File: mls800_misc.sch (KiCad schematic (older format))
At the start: 18 parts, among them SW10 SW_TACT_LED_2, SW11 SW_TACT_LED_2, SW4 SW_TACT_LED_2, SW5 SW_TACT_LED_2, SW6 SW_TACT_LED_2, SW7 SW_TACT_LED_2, SW8 SW_TACT_LED_2, SW9 SW_TACT_LED_2, U4 MCP23017

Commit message: MLS800 : fixed missing components
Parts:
- SW10, SW11, SW4, SW5, SW6, SW7, SW8, SW9: value SW_TACT_LED_2 -> SW_TACT_LED; symbol SW_TACT_LED_2 -> SW_TACT_LED
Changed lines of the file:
@@
 LIBS:custom-device
 LIBS:custom-display
+LIBS:custom-micro
 LIBS:mls800-cache
 EELAYER 24 0
@@
 	3600 4850 3700 4950
 $Comp
-L SW_TACT_LED_2 SW4
+L SW_TACT_LED SW4
 U 2 1 53B9BB32
 P 4900 1300
 F 0 "SW4" H 4700 1200 60  0000 C CNN
-F 1 "SW_TACT_LED_2" H 4950 1200 60  0001 C CNN
+F 1 "SW_TACT_LED" H 4950 1200 60  0001 C CNN
 F 2 "" H 4900 1300 60  0000 C CNN
 F 3 "" H 4900 1300 60  0000 C CNN
@@
 $EndComp
 $Comp
-L SW_TACT_LED_2 SW4
+L SW_TACT_LED SW4
 U 1 1 53B9BB41
 P 4900 1100
 F 0 "SW4" H 4700 1250 60  0000 C CNN
-F 1 "SW_TACT_LED_2" H 4950 1000 60  0001 C CNN
+F 1 "SW_TACT_LED" H 4950 1000 60  0001 C CNN
 F 2 "" H 4900 1100 60  0000 C CNN
 F 3 "" H 4900 1100 60  0000 C CNN
@@
 $EndComp
 $Comp
-L SW_TACT_LED_2 SW5
+L SW_TACT_LED SW5
 U 2 1 53B9BB96
 P 4900 1850
 F 0 "SW5" H 4700 1750 60  0000 C CNN
-F 1 "SW_TACT_LED_2" H 4950 1750 60  0001 C CNN
+F 1 "SW_TACT_LED" H 4950 1750 60  0001 C CNN
 F 2 "" H 4900 1850 60  0000 C CNN
 F 3 "" H 4900 1850 60  0000 C CNN
@@
 $EndComp
 $Comp
-L SW_TACT_LED_2 SW5
+L SW_TACT_LED SW5
 U 1 1 53B9BB9C
 P 4900 1650
 F 0 "SW5" H 4700 1800 60  0000 C CNN
-F 1 "SW_TACT_LED_2" H 4950 1550 60  0001 C CNN
+F 1 "SW_TACT_LED" H 4950 1550 60  0001 C CNN
 F 2 "" H 4900 1650 60  0000 C CNN
 F 3 "" H 4900 1650 60  0000 C CNN
@@
 $EndComp
 $Comp
-L SW_TACT_LED_2 SW6
+L SW_TACT_LED SW6
 U 2 1 53B9BBAC
 P 4900 2400
 F 0 "SW6" H 4700 2300 60  0000 C CNN
-F 1 "SW_TACT_LED_2" H 4950 2300 60  0001 C CNN
+F 1 "SW_TACT_LED" H 4950 2300 60  0001 C CNN
 F 2 "" H 4900 2400 60  0000 C CNN
 F 3 "" H 4900 2400 60  0000 C CNN
@@
 $EndComp
 $Comp
-L SW_TACT_LED_2 SW6
+L SW_TACT_LED SW6
 U 1 1 53B9BBB2
 P 4900 2200
 F 0 "SW6" H 4700 2350 60  0000 C CNN
-F 1 "SW_TACT_LED_2" H 4950 2100 60  0001 C CNN
+F 1 "SW_TACT_LED" H 4950 2100 60  0001 C CNN
 F 2 "" H 4900 2200 60  0000 C CNN
 F 3 "" H 4900 2200 60  0000 C CNN
@@
 $EndComp
 $Comp
-L SW_TACT_LED_2 SW7
+L SW_TACT_LED SW7
 U 2 1 53B9BBB8
 P 4900 2950
 F 0 "SW7" H 4700 2850 60  0000 C CNN
-F 1 "SW_TACT_LED_2" H 4950 2850 60  0001 C CNN
+F 1 "SW_TACT_LED" H 4950 2850 60  0001 C CNN
 F 2 "" H 4900 2950 60  0000 C CNN
 F 3 "" H 4900 2950 60  0000 C CNN
@@
 $EndComp
 $Comp
-L SW_TACT_LED_2 SW7
+L SW_TACT_LED SW7
 U 1 1 53B9BBBE
 P 4900 2750
 F 0 "SW7" H 4700 2900 60  0000 C CNN
-F 1 "SW_TACT_LED_2" H 4950 2650 60  0001 C CNN
+F 1 "SW_TACT_LED" H 4950 2650 60  0001 C CNN
 F 2 "" H 4900 2750 60  0000 C CNN
 F 3 "" H 4900 2750 60  0000 C CNN
@@
 $EndComp
 $Comp
-L SW_TACT_LED_2 SW8
+L SW_TACT_LED SW8
 U 2 1 53B9BBC4
 P 4900 3500
 F 0 "SW8" H 4700 3400 60  0000 C CNN
-F 1 "SW_TACT_LED_2" H 4950 3400 60  0001 C CNN
+F 1 "SW_TACT_LED" H 4950 3400 60  0001 C CNN
 F 2 "" H 4900 3500 60  0000 C CNN
 F 3 "" H 4900 3500 60  0000 C CNN
@@
 $EndComp
 $Comp
-L SW_TACT_LED_2 SW8
+L SW_TACT_LED SW8
 U 1 1 53B9BBCA
 P 4900 3300
 F 0 "SW8" H 4700 3450 60  0000 C CNN
-F 1 "SW_TACT_LED_2" H 4950 3200 60  0001 C CNN
+F 1 "SW_TACT_LED" H 4950 3200 60  0001 C CNN
 F 2 "" H 4900 3300 60  0000 C CNN
 F 3 "" H 4900 3300 60  0000 C CNN
@@
 $EndComp
 $Comp
-L SW_TACT_LED_2 SW9
+L SW_TACT_LED SW9
 U 2 1 53B9BBD0
 P 4900 4050
 F 0 "SW9" H 4700 3950 60  0000 C CNN
-F 1 "SW_TACT_LED_2" H 4950 3950 60  0001 C CNN
+F 1 "SW_TACT_LED" H 4950 3950 60  0001 C CNN
 F 2 "" H 4900 4050 60  0000 C CNN
 F 3 "" H 4900 4050 60  0000 C CNN
@@
 $EndComp
 $Comp
-L SW_TACT_LED_2 SW9
+L SW_TACT_LED SW9
 U 1 1 53B9BBD6
 P 4900 3850
 F 0 "SW9" H 4700 4000 60  0000 C CNN
-F 1 "SW_TACT_LED_2" H 4950 3750 60  0001 C CNN
+F 1 "SW_TACT_LED" H 4950 3750 60  0001 C CNN
 F 2 "" H 4900 3850 60  0000 C CNN
 F 3 "" H 4900 3850 60  0000 C CNN
@@
 $EndComp
 $Comp
-L SW_TACT_LED_2 SW10
+L SW_TACT_LED SW10
 U 2 1 53B9BBDC
 P 4900 4600
 F 0 "SW10" H 4700 4500 60  0000 C CNN
-F 1 "SW_TACT_LED_2" H 4950 4500 60  0001 C CNN
+F 1 "SW_TACT_LED" H 4950 4500 60  0001 C CNN
 F 2 "" H 4900 4600 60  0000 C CNN
 F 3 "" H 4900 4600 60  0000 C CNN
@@
 $EndComp
 $Comp
-L SW_TACT_LED_2 SW10
+L SW_TACT_LED SW10
 U 1 1 53B9BBE2
 P 4900 4400
 F 0 "SW10" H 4700 4550 60  0000 C CNN
-F 1 "SW_TACT_LED_2" H 4950 4300 60  0001 C CNN
+F 1 "SW_TACT_LED" H 4950 4300 60  0001 C CNN
 F 2 "" H 4900 4400 60  0000 C CNN
 F 3 "" H 4900 4400 60  0000 C CNN
@@
 $EndComp
 $Comp
-L SW_TACT_LED_2 SW11
+L SW_TACT_LED SW11
 U 2 1 53B9BBE8
 P 4900 5150
 F 0 "SW11" H 4700 5050 60  0000 C CNN
-F 1 "SW_TACT_LED_2" H 4950 5050 60  0001 C CNN
+F 1 "SW_TACT_LED" H 4950 5050 60  0001 C CNN
 F 2 "" H 4900 5150 60  0000 C CNN
 F 3 "" H 4900 5150 60  0000 C CNN
@@
 $EndComp
 $Comp
-L SW_TACT_LED_2 SW11
+L SW_TACT_LED SW11
 U 1 1 53B9BBEE
 P 4900 4950
 F 0 "SW11" H 4700 5100 60  0000 C CNN
-F 1 "SW_TACT_LED_2" H 4950 4850 60  0001 C CNN
+F 1 "SW_TACT_LED" H 4950 4850 60  0001 C CNN
 F 2 "" H 4900 4950 60  0000 C CNN
 F 3 "" H 4900 4950 60  0000 C CNN

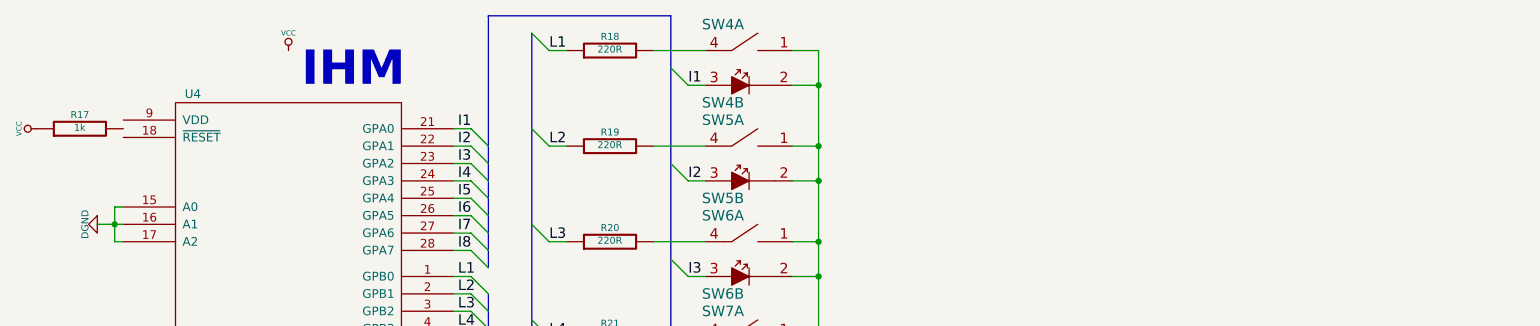
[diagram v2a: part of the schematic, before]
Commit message: MLS800 : fixed broken layout
MLS800 : added some comments on schematics rather than using a notepad :)
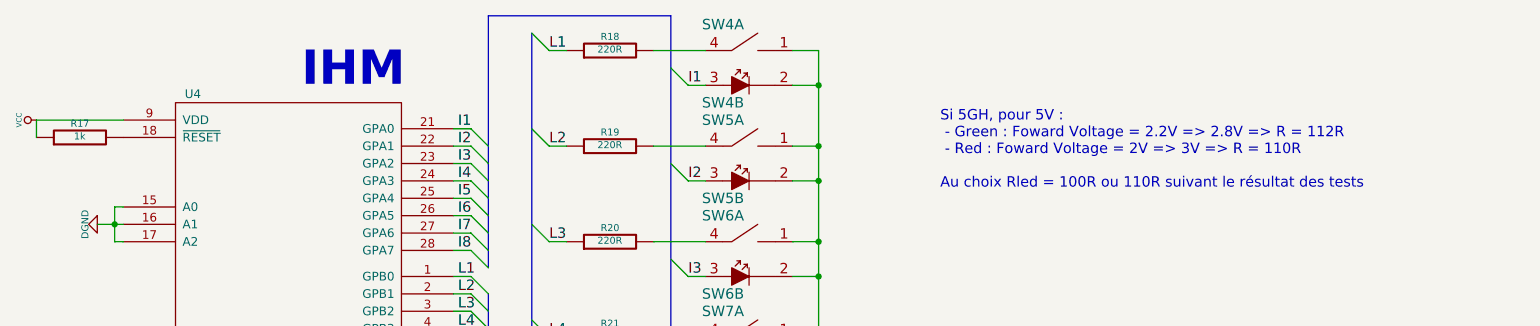
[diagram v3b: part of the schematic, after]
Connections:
- net VCC: now also U4.9 (VDD)
- net at U4.18 (~RESET): now also R17.2
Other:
- note added: "Si 5GH, pour 5V : \n - Green : Foward Voltage = 2.2V => 2.8V => R = 112R\n - Red : Foward Voltage = 2V => 3V => R = 110R\n\nAu choix Rled = 100R ou 110R suivant le résultat des tests"
- moved on the sheet: R17
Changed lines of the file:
@@
 L VCC #PWR045
 U 1 1 5350562C
-P 2200 1100
-F 0 "#PWR045" H 2200 1200 30  0001 C CNN
-F 1 "VCC" H 2200 1200 30  0000 C CNN
-F 2 "" H 2200 1100 60  0000 C CNN
-F 3 "" H 2200 1100 60  0000 C CNN
-	1    2200 1100
-	1    0    0    -1
+P 750 1500
+F 0 "#PWR045" H 750 1600 30  0001 C CNN
+F 1 "VCC" H 750 1600 30  0000 C CNN
+F 2 "" H 750 1500 60  0000 C CNN
+F 3 "" H 750 1500 60  0000 C CNN
+	1    750  1500
+	0    -1   -1   0
 $EndComp
 $Comp
 L R R17
 U 1 1 53505640
-P 1000 1550
-F 0 "R17" V 1080 1550 40  0000 C CNN
-F 1 "1k" V 1007 1551 40  0000 C CNN
-F 2 "Resistors_SMD:R_0805_HandSoldering" V 930 1550 30  0001 C CNN
-F 3 "~" H 1000 1550 30  0000 C CNN
-	1    1000 1550
+P 1000 1600
+F 0 "R17" V 1080 1600 40  0000 C CNN
+F 1 "1k" V 1007 1601 40  0000 C CNN
+F 2 "Resistors_SMD:R_0805_HandSoldering" V 930 1600 30  0001 C CNN
+F 3 "~" H 1000 1600 30  0000 C CNN
+	1    1000 1600
 	0    -1   -1   0
 $EndComp
@@
 	0    1    1    0
 $EndComp
-$Comp
-L VCC #PWR?
-U 1 1 543C72E7
-P 750 1550
-F 0 "#PWR?" H 750 1650 30  0001 C CNN
-F 1 "VCC" H 750 1650 30  0000 C CNN
-F 2 "" H 750 1550 60  0000 C CNN
-F 3 "" H 750 1550 60  0000 C CNN
-	1    750  1550
-	0    -1   -1   0
-$EndComp
+Text Notes 5950 1900 0    60   ~ 0
+Si 5GH, pour 5V : \n - Green : Foward Voltage = 2.2V => 2.8V => R = 112R\n - Red : Foward Voltage = 2V => 3V => R = 110R\n\nAu choix Rled = 100R ou 110R suivant le résultat des tests
+Wire Wire Line
+	750  1500 1250 1500
+Wire Wire Line
+	750  1600 750  1500
 $EndSCHEMATC

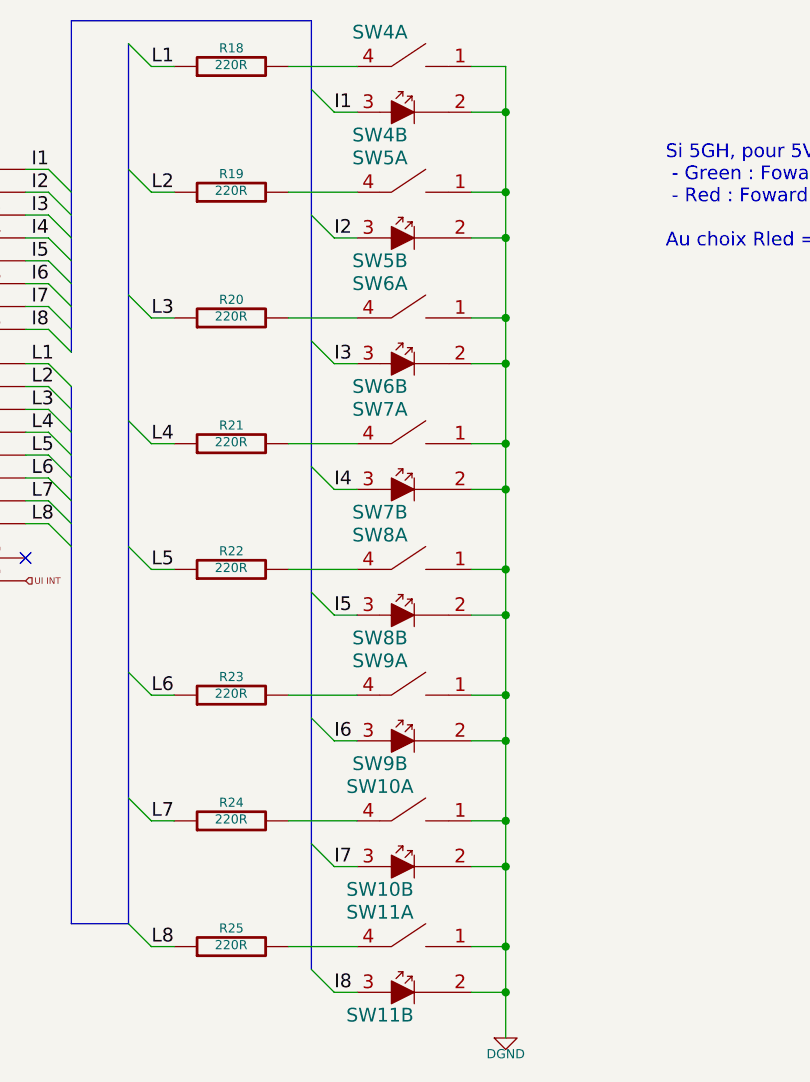
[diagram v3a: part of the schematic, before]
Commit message: MLS800 : disabled switch tact led "interchangeable" units => fixed annotations
MLS800 : front panel schematic seems to be completed
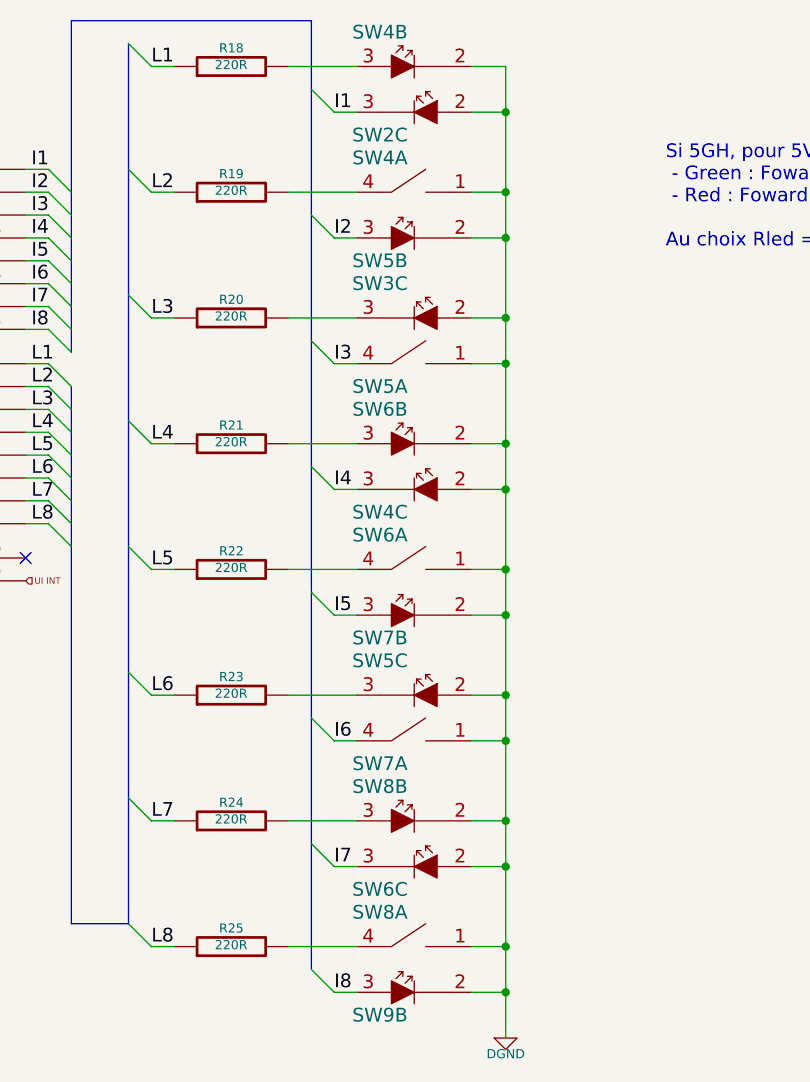
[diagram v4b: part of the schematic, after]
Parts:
- renumbered SW4 to SW2, SW6 to SW3, SW5 to SW4, SW7 to SW4, SW6 to SW5, SW9 to SW5, SW7 to SW6, SW8 to SW6, SW10 to SW6, SW8 to SW7, SW9 to SW7, SW10 to SW8, SW11 to SW8, SW11 to SW9
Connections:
- net DGND: now also SW3.2, SW4.2, SW5.1, SW5.2, SW6.2, SW7.1, SW8.2; no longer SW3.1, SW4.1, SW5.1, SW5.2, SW6.1, SW7.2, SW8.1
- net I3: now also SW5.4; no longer SW5.3
- net I6: now also SW7.4; no longer SW7.3
- net at R18.2: now also SW4.3; no longer SW4.4
- net at R20.2: now also SW3.3; no longer SW3.4
- net at R21.2: now also SW6.3; no longer SW6.4
- net at R23.2: now also SW5.3; no longer SW5.4
- net at R24.2: now also SW8.3; no longer SW8.4
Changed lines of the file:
@@
 $EndComp
 $Comp
-L VCC #PWR045
+L VCC #PWR43
 U 1 1 5350562C
 P 750 1500
-F 0 "#PWR045" H 750 1600 30  0001 C CNN
+F 0 "#PWR43" H 750 1600 30  0001 C CNN
 F 1 "VCC" H 750 1600 30  0000 C CNN
 F 2 "" H 750 1500 60  0000 C CNN
@@
 	3600 4850 3700 4950
 $Comp
-L SW_TACT_LED SW4
-U 2 1 53B9BB32
+L SW_TACT_LED SW2
+U 3 1 53B9BB32
 P 4900 1300
-F 0 "SW4" H 4700 1200 60  0000 C CNN
+F 0 "SW2" H 4700 1200 60  0000 C CNN
 F 1 "SW_TACT_LED" H 4950 1200 60  0001 C CNN
 F 2 "" H 4900 1300 60  0000 C CNN
 F 3 "" H 4900 1300 60  0000 C CNN
-	2    4900 1300
+	3    4900 1300
 	1    0    0    -1
 $EndComp
 $Comp
 L SW_TACT_LED SW4
-U 1 1 53B9BB41
+U 2 1 53B9BB41
 P 4900 1100
 F 0 "SW4" H 4700 1250 60  0000 C CNN
@@
 F 2 "" H 4900 1100 60  0000 C CNN
 F 3 "" H 4900 1100 60  0000 C CNN
-	1    4900 1100
+	2    4900 1100
 	1    0    0    -1
 $EndComp
@@
 $EndComp
 $Comp
-L SW_TACT_LED SW5
+L SW_TACT_LED SW4
 U 1 1 53B9BB9C
 P 4900 1650
-F 0 "SW5" H 4700 1800 60  0000 C CNN
+F 0 "SW4" H 4700 1800 60  0000 C CNN
 F 1 "SW_TACT_LED" H 4950 1550 60  0001 C CNN
 F 2 "" H 4900 1650 60  0000 C CNN
@@
 $EndComp
 $Comp
-L SW_TACT_LED SW6
-U 2 1 53B9BBAC
+L SW_TACT_LED SW5
+U 1 1 53B9BBAC
 P 4900 2400
-F 0 "SW6" H 4700 2300 60  0000 C CNN
+F 0 "SW5" H 4700 2300 60  0000 C CNN
 F 1 "SW_TACT_LED" H 4950 2300 60  0001 C CNN
 F 2 "" H 4900 2400 60  0000 C CNN
 F 3 "" H 4900 2400 60  0000 C CNN
-	2    4900 2400
-	1    0    0    -1
-$EndComp
-$Comp
-L SW_TACT_LED SW6
-U 1 1 53B9BBB2
+	1    4900 2400
+	1    0    0    -1
+$EndComp
+$Comp
+L SW_TACT_LED SW3
+U 3 1 53B9BBB2
 P 4900 2200
-F 0 "SW6" H 4700 2350 60  0000 C CNN
+F 0 "SW3" H 4700 2350 60  0000 C CNN
 F 1 "SW_TACT_LED" H 4950 2100 60  0001 C CNN
 F 2 "" H 4900 2200 60  0000 C CNN
 F 3 "" H 4900 2200 60  0000 C CNN
-	1    4900 2200
-	1    0    0    -1
-$EndComp
-$Comp
-L SW_TACT_LED SW7
-U 2 1 53B9BBB8
+	3    4900 2200
+	1    0    0    -1
+$EndComp
+$Comp
+L SW_TACT_LED SW4
+U 3 1 53B9BBB8
 P 4900 2950
-F 0 "SW7" H 4700 2850 60  0000 C CNN
+F 0 "SW4" H 4700 2850 60  0000 C CNN
 F 1 "SW_TACT_LED" H 4950 2850 60  0001 C CNN
 F 2 "" H 4900 2950 60  0000 C CNN
 F 3 "" H 4900 2950 60  0000 C CNN
-	2    4900 2950
-	1    0    0    -1
-$EndComp
-$Comp
-L SW_TACT_LED SW7
-U 1 1 53B9BBBE
+	3    4900 2950
+	1    0    0    -1
+$EndComp
+$Comp
+L SW_TACT_LED SW6
+U 2 1 53B9BBBE
 P 4900 2750
-F 0 "SW7" H 4700 2900 60  0000 C CNN
+F 0 "SW6" H 4700 2900 60  0000 C CNN
 F 1 "SW_TACT_LED" H 4950 2650 60  0001 C CNN
 F 2 "" H 4900 2750 60  0000 C CNN
 F 3 "" H 4900 2750 60  0000 C CNN
-	1    4900 2750
-	1    0    0    -1
-$EndComp
-$Comp
-L SW_TACT_LED SW8
+	2    4900 2750
+	1    0    0    -1
+$EndComp
+$Comp
+L SW_TACT_LED SW7
 U 2 1 53B9BBC4
 P 4900 3500
-F 0 "SW8" H 4700 3400 60  0000 C CNN
+F 0 "SW7" H 4700 3400 60  0000 C CNN
 F 1 "SW_TACT_LED" H 4950 3400 60  0001 C CNN
 F 2 "" H 4900 3500 60  0000 C CNN
@@
 $EndComp
 $Comp
-L SW_TACT_LED SW8
+L SW_TACT_LED SW6
 U 1 1 53B9BBCA
 P 4900 3300
-F 0 "SW8" H 4700 3450 60  0000 C CNN
+F 0 "SW6" H 4700 3450 60  0000 C CNN
 F 1 "SW_TACT_LED" H 4950 3200 60  0001 C CNN
 F 2 "" H 4900 3300 60  0000 C CNN
@@
 $EndComp
 $Comp
-L SW_TACT_LED SW9
-U 2 1 53B9BBD0
+L SW_TACT_LED SW7
+U 1 1 53B9BBD0
 P 4900 4050
-F 0 "SW9" H 4700 3950 60  0000 C CNN
+F 0 "SW7" H 4700 3950 60  0000 C CNN
 F 1 "SW_TACT_LED" H 4950 3950 60  0001 C CNN
 F 2 "" H 4900 4050 60  0000 C CNN
 F 3 "" H 4900 4050 60  0000 C CNN
-	2    4900 4050
-	1    0    0    -1
-$EndComp
-$Comp
-L SW_TACT_LED SW9
-U 1 1 53B9BBD6
+	1    4900 4050
+	1    0    0    -1
+$EndComp
+$Comp
+L SW_TACT_LED SW5
+U 3 1 53B9BBD6
 P 4900 3850
-F 0 "SW9" H 4700 4000 60  0000 C CNN
+F 0 "SW5" H 4700 4000 60  0000 C CNN
 F 1 "SW_TACT_LED" H 4950 3750 60  0001 C CNN
 F 2 "" H 4900 3850 60  0000 C CNN
 F 3 "" H 4900 3850 60  0000 C CNN
-	1    4900 3850
-	1    0    0    -1
-$EndComp
-$Comp
-L SW_TACT_LED SW10
-U 2 1 53B9BBDC
+	3    4900 3850
+	1    0    0    -1
+$EndComp
+$Comp
+L SW_TACT_LED SW6
+U 3 1 53B9BBDC
 P 4900 4600
-F 0 "SW10" H 4700 4500 60  0000 C CNN
+F 0 "SW6" H 4700 4500 60  0000 C CNN
 F 1 "SW_TACT_LED" H 4950 4500 60  0001 C CNN
 F 2 "" H 4900 4600 60  0000 C CNN
 F 3 "" H 4900 4600 60  0000 C CNN
-	2    4900 4600
-	1    0    0    -1
-$EndComp
-$Comp
-L SW_TACT_LED SW10
-U 1 1 53B9BBE2
+	3    4900 4600
+	1    0    0    -1
+$EndComp
+$Comp
+L SW_TACT_LED SW8
+U 2 1 53B9BBE2
 P 4900 4400
-F 0 "SW10" H 4700 4550 60  0000 C CNN
+F 0 "SW8" H 4700 4550 60  0000 C CNN
 F 1 "SW_TACT_LED" H 4950 4300 60  0001 C CNN
 F 2 "" H 4900 4400 60  0000 C CNN
 F 3 "" H 4900 4400 60  0000 C CNN
-	1    4900 4400
-	1    0    0    -1
-$EndComp
-$Comp
-L SW_TACT_LED SW11
+	2    4900 4400
+	1    0    0    -1
+$EndComp
+$Comp
+L SW_TACT_LED SW9
 U 2 1 53B9BBE8
 P 4900 5150
-F 0 "SW11" H 4700 5050 60  0000 C CNN
+F 0 "SW9" H 4700 5050 60  0000 C CNN
 F 1 "SW_TACT_LED" H 4950 5050 60  0001 C CNN
 F 2 "" H 4900 5150 60  0000 C CNN
@@
 $EndComp
 $Comp
-L SW_TACT_LED SW11
+L SW_TACT_LED SW8
 U 1 1 53B9BBEE
 P 4900 4950
-F 0 "SW11" H 4700 5100 60  0000 C CNN
+F 0 "SW8" H 4700 5100 60  0000 C CNN
 F 1 "SW_TACT_LED" H 4950 4850 60  0001 C CNN
 F 2 "" H 4900 4950 60  0000 C CNN
@@
 Connection ~ 5250 1300
 $Comp
-L DGND #PWR046
+L DGND #PWR46
 U 1 1 53F19F43
 P 5250 5350
-F 0 "#PWR046" H 5250 5350 40  0001 C CNN
+F 0 "#PWR46" H 5250 5350 40  0001 C CNN
 F 1 "DGND" H 5250 5280 40  0000 C CNN
 F 2 "" H 5250 5350 60  0000 C CNN
@@
 $EndComp
 $Comp
-L DGND #PWR047
+L DGND #PWR45
 U 1 1 53F19F5C
 P 2200 3800
-F 0 "#PWR047" H 2200 3800 40  0001 C CNN
+F 0 "#PWR45" H 2200 3800 40  0001 C CNN
 F 1 "DGND" H 2200 3730 40  0000 C CNN
 F 2 "" H 2200 3800 60  0000 C CNN
@@
 $EndComp
 $Comp
-L DGND #PWR048
+L DGND #PWR44
 U 1 1 53F19F6B
 P 1100 2100
-F 0 "#PWR048" H 1100 2100 40  0001 C CNN
+F 0 "#PWR44" H 1100 2100 40  0001 C CNN
 F 1 "DGND" H 1100 2030 40  0000 C CNN
 F 2 "" H 1100 2100 60  0000 C CNN
